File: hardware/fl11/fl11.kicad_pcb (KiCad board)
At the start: 2 copper layers, 187 x 48 mm, 67 parts, among them J1 USB-C 16P, J2_1 TOUCH_SENSE, J2_2 GND, J3_1 TOUCH_SENSE, J3_2 GND, Q1 AO3401A, SW1 BOOT, U1 ESP32-C3-MINI-1-N4, U2 SN74AHCT1G125, U3 AP2112K-3.3, U4 USBLC6-2SC6

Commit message: FL-11 rev E: comb touch electrodes, a fallback header, and the silkscreen that was missing
Correction first: the rev C and rev D commit messages said the silkscreen carried
the name, version and repo URL. It did not. The silk() calls were lost in an
earlier edit and no identity text was on the board at all. They are there now,
verified in the render: name, version, copyright and repo URL, with the
copyright repeated on the snap-off pad so it survives the break.

Interdigitated electrodes, for sensing through plastic. Two solid plates couple
mostly through the overlay's thickness; a comb pushes the field out of the
surface as fringing, which is what a finger behind a cover actually intercepts.
Seven 1.1 mm fingers per electrode on a 3.0 mm pitch, so a ~10 mm fingertip
always spans several SENSE/GND pairs and the delta stays large through a thin
cover instead of collapsing.

J4 gives the escape hatch: four pads, 5V / 3V3 / GND / SIG, next to the break.
A TTP223-class module needs a supply, a ground and one digital output, and
TOUCH_GPIO doubles as that input because touch.py's pin is plain digital rather
than ADC. Both rails are brought out since those modules come in 3.3 V and 5 V
variants. Zero placements, zero BOM lines.

DRC 0 errors, 71 footprints, single-sided, 55 connections still unrouted.

Co-Authored-By: Claude Opus 5 (1M context) <noreply@anthropic.com>
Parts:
- added J4_1: 5V, TestPoint_Pad_D1.0mm, F.Cu at (118.5, 31.0)
- added J4_2: 3V3, TestPoint_Pad_D1.0mm, F.Cu at (118.5, 33.5)
- added J4_3: GND, TestPoint_Pad_D1.0mm, F.Cu at (118.5, 36.0)
- added J4_4: SIG, TestPoint_Pad_D1.0mm, F.Cu at (118.5, 38.5)
- moved TP2 18.6 mm to (109.5, 47.0)
- moved TP3 15.0 mm to (112.5, 47.0)
- moved J2_2 5.00 mm to (117.5, 46.0)
- moved J3_2 5.00 mm to (128.0, 46.0)
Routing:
- net TOUCH_SENSE: track 26.0 -> 23.0 mm
- net GND: track 12.5 -> 9.50 mm
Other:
- outline, holes or cut-outs redrawn
- board text added: "5V 3V3 GND SIG"
- board text added: "CUT TRACES, THEN BEND"
- board text added: "FL-11 rev E TOUCH"
- board text added: "FL-11 rev E · © 2026 Fionn Ferreira"
- board text added: "LINKED FRIEND LIGHTS"
- board text added: "github.com/fionnf/linked-friend-lights-public"
- board text added: "© 2026 Fionn Ferreira"

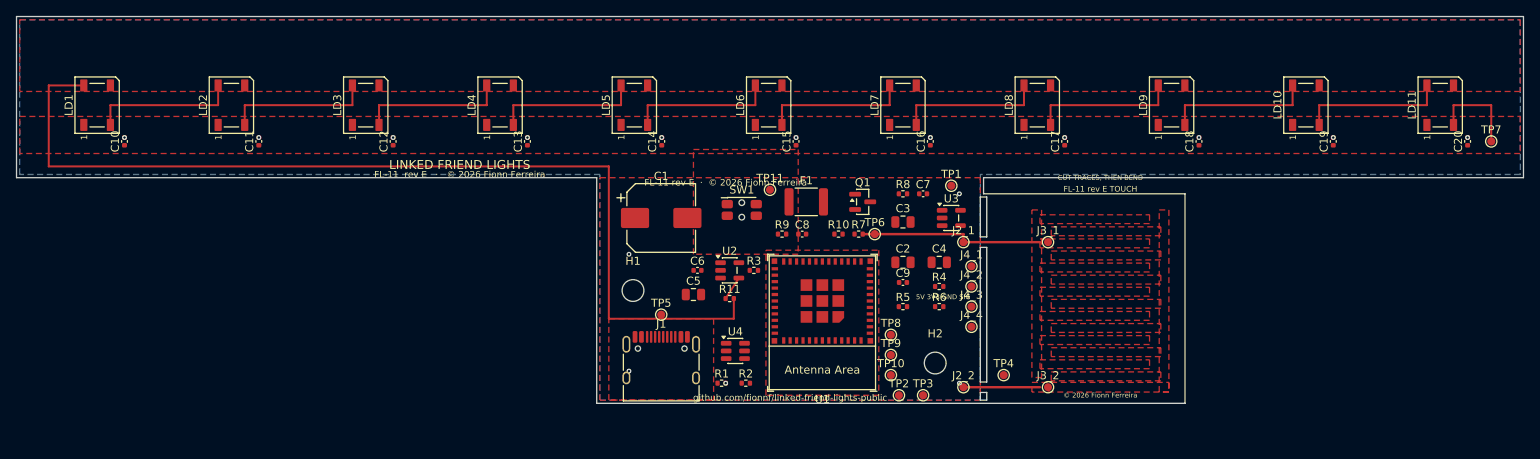
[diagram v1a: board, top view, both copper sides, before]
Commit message: FL-11 rev F: 20 LEDs, and two silent routing bugs fixed
20 LEDs at 8.33333 mm, which is 120 LEDs/m and a standard strip density.
Twenty at that pitch give a lit zone of exactly 166.67 mm -- the same lamp
length as eleven at 60/m, at double the density, so the dots blend. The
outline is unchanged; LED20 lands at x=168.33 on a 187 mm strip.

F1 becomes 3A hold / 5A trip. Twenty LEDs put worst case at ~2.25 A and the
2 A part would nuisance-trip. Same 1812 footprint. Two consequences that are
NOT handled and must not be skipped: the supply has to be 3 A rather than the
2.4 A the cost model assumed, and the copper was sized for 1.6 A -- the 4.6 mm
pour probably carries 2.5 A but that sum has not been redone.

Two routing bugs, both silent, both found only by checking the unconnected
count rather than trusting DRC:

- The DOUT-to-DIN loop was still bounded at 11 after the LED count changed, so
  LEDs 11 through 20 had no data connection at all. Ten hops routed, nine
  missing, zero DRC errors.
- The bypass caps' 5 V pads sat 0.4 mm from the pour edge, too close for
  thermal spokes to form, leaving 23 of them floating. Moved fully inside the
  pour and rotated flat, since at 8.33 mm pitch a vertical 0402 does not fit
  in a 4.6 mm pour with spoke clearance.

Now: all 19 hops routed, all 20 LEDs and all 20 caps connected, 0 DRC errors.
54 endpoints remain unrouted and all of them are in the bulge.

Silkscreen text pulled clear of every board edge and off the notch void.

Co-Authored-By: Claude Opus 5 (1M context) <noreply@anthropic.com>
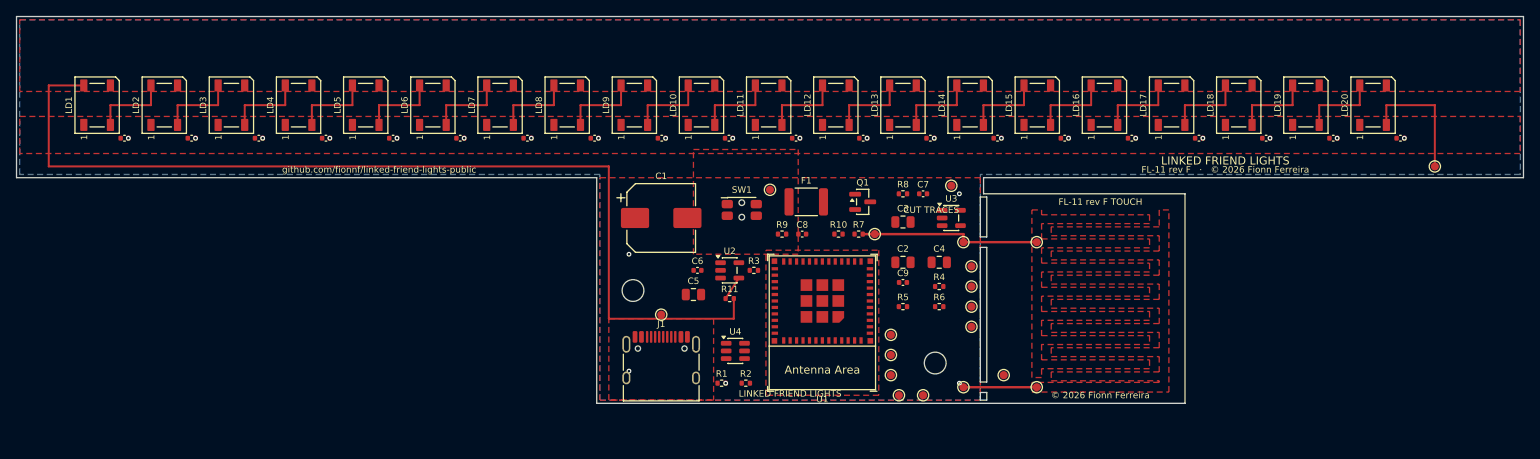
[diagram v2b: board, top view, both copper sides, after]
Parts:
- added C21: 100nF, C_0402_1005Metric, F.Cu at (105.1, 15.1)
- added C22: 100nF, C_0402_1005Metric, F.Cu at (113.4, 15.1)
- added C23: 100nF, C_0402_1005Metric, F.Cu at (121.7, 15.1)
- added C24: 100nF, C_0402_1005Metric, F.Cu at (130.1, 15.1)
- added C25: 100nF, C_0402_1005Metric, F.Cu at (138.4, 15.1)
- added C26: 100nF, C_0402_1005Metric, F.Cu at (146.7, 15.1)
- added C27: 100nF, C_0402_1005Metric, F.Cu at (155.1, 15.1)
- added C28: 100nF, C_0402_1005Metric, F.Cu at (163.4, 15.1)
- added C29: 100nF, C_0402_1005Metric, F.Cu at (171.7, 15.1)
- added LD12: SK6812RGBW, LED_WS2812B_PLCC4_5.0x5.0mm_P3.2mm, F.Cu at (101.7, 11.0)
- added LD13: SK6812RGBW, LED_WS2812B_PLCC4_5.0x5.0mm_P3.2mm, F.Cu at (110.0, 11.0)
- added LD14: SK6812RGBW, LED_WS2812B_PLCC4_5.0x5.0mm_P3.2mm, F.Cu at (118.3, 11.0)
- added LD15: SK6812RGBW, LED_WS2812B_PLCC4_5.0x5.0mm_P3.2mm, F.Cu at (126.7, 11.0)
- added LD16: SK6812RGBW, LED_WS2812B_PLCC4_5.0x5.0mm_P3.2mm, F.Cu at (135.0, 11.0)
- added LD17: SK6812RGBW, LED_WS2812B_PLCC4_5.0x5.0mm_P3.2mm, F.Cu at (143.3, 11.0)
- added LD18: SK6812RGBW, LED_WS2812B_PLCC4_5.0x5.0mm_P3.2mm, F.Cu at (151.7, 11.0)
- added LD19: SK6812RGBW, LED_WS2812B_PLCC4_5.0x5.0mm_P3.2mm, F.Cu at (160.0, 11.0)
- added LD20: SK6812RGBW, LED_WS2812B_PLCC4_5.0x5.0mm_P3.2mm, F.Cu at (168.3, 11.0)
- F1: value PPTC 2A/4A -> PPTC 3A/5A
- moved C20 83.3 mm to (96.7, 15.1), turned to 0 degrees
- moved LD11 83.3 mm to (93.3, 11.0)
- moved C19 75.0 mm to (88.4, 15.1), turned to 0 degrees
- moved LD10 75.0 mm to (85.0, 11.0)
- moved C18 66.7 mm to (80.1, 15.1), turned to 0 degrees
- moved LD9 66.7 mm to (76.7, 11.0)
- moved C17 58.3 mm to (71.7, 15.1), turned to 0 degrees
- moved LD8 58.3 mm to (68.3, 11.0)
- moved C16 50.0 mm to (63.4, 15.1), turned to 0 degrees
- moved LD7 50.0 mm to (60.0, 11.0)
- moved C15 41.7 mm to (55.1, 15.1), turned to 0 degrees
- moved LD6 41.7 mm to (51.7, 11.0)
- moved C14 33.3 mm to (46.7, 15.1), turned to 0 degrees
- moved LD5 33.3 mm to (43.3, 11.0)
- moved C13 25.0 mm to (38.4, 15.1), turned to 0 degrees
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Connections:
- LD11 pad 2: LD11_DOUT -> D_11_12
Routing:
- net D_19_20: track 0.00 -> 9.93 mm
- net D_18_19: track 0.00 -> 9.93 mm
- net D_16_17: track 0.00 -> 9.93 mm
- net D_15_16: track 0.00 -> 9.93 mm
- net D_14_15: track 0.00 -> 9.93 mm
- net D_13_14: track 0.00 -> 9.93 mm
- net D_11_12: track 0.00 -> 9.93 mm
- net D_12_13: track 0.00 -> 9.93 mm
- net D_17_18: track 0.00 -> 9.93 mm
- net D_9_10: track 18.3 -> 9.93 mm
- net D_8_9: track 18.3 -> 9.93 mm
- net D_6_7: track 18.3 -> 9.93 mm
- net D_5_6: track 18.3 -> 9.93 mm
- net D_3_4: track 18.3 -> 9.93 mm
- net D_2_3: track 18.3 -> 9.93 mm
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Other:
- board text added: "CUT TRACES"
- board text added: "FL-11 rev F TOUCH"
- board text added: "FL-11 rev F · © 2026 Fionn Ferreira"
- board text removed: "5V 3V3 GND SIG"
- board text removed: "CUT TRACES, THEN BEND"
- board text removed: "FL-11 rev E TOUCH"
- board text removed: "FL-11 rev E · © 2026 Fionn Ferreira"

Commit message: FL-11 rev G: 15 warm-white LEDs, and the board is routed
15 LEDs at 11.13333 mm. The lit zone stays at exactly 167.00 mm so the lamp
length does not move, and worst case drops to ~1.69 A -- back under the 2 A
PPTC and inside a 2.4 A supply. F1 returns to the 2A/4A part, and both
warnings rev F carried are withdrawn: at 1.69 A the section 5.5 copper sizing
holds with margin.

The LED part was already warm white and now says so. C5378724 is
SKC6812RGBW-WS; the -NW neutral part is C5348912 and would fight
BASE_WARM_WHITE, which is the basis of colour.py's whole model.

Routing is complete: zero unconnected component pads, 345 tracks and 202 vias,
865 mm of copper, 279 segments on F.Cu and 66 on B.Cu.

The bulge was finished with freerouting 2.3.0 through KiCad's Specctra
DSN/SES path. Section 7.9 says not to autoroute and that stands for the three
nets it names, so SENSE, the LED chain, the tab bridges and the pours were
hand-routed first and the router had to work around them. It did: SENSE still
has zero vias and still never crosses the LED data channel.

finish_routing.py fixes what the router got wrong -- 0.15 mm tracks widened to
the 0.20 mm floor, 146 collision-checked stitching vias, ties for the
priority-3 patches the pour clips around, and floating island removal.

Two DRC errors remain and both want a human in the PCB editor, not a script:
a clearance in the 0.5 mm-pitch USB-C fan-out where D+ and D- interleave,
which is precisely the case section 6.2 means by routing D± by hand, and a
STRAP2 via sitting too close to a +3V3 track. Neither is a connectivity
failure.

Co-Authored-By: Claude Opus 5 (1M context) <noreply@anthropic.com>
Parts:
- removed C25, C26, C27, C28, C29: 100nF, C_0402_1005Metric
- removed LD16, LD17, LD18, LD19, LD20: SK6812RGBW, LED_WS2812B_PLCC4_5.0x5.0mm_P3.2mm
- F1: value PPTC 3A/5A -> PPTC 2A/4A
- moved C24 39.2 mm to (169.3, 15.1)
- moved LD15 39.2 mm to (165.9, 11.0)
- moved LD14 36.4 mm to (154.7, 11.0)
- moved C23 36.4 mm to (158.1, 15.1)
- moved C22 33.6 mm to (147.0, 15.1)
- moved LD13 33.6 mm to (143.6, 11.0)
- moved C21 30.8 mm to (135.9, 15.1)
- moved LD12 30.8 mm to (132.5, 11.0)
- moved C20 28.0 mm to (124.7, 15.1)
- moved LD11 28.0 mm to (121.3, 11.0)
- moved TP10 27.4 mm to (100.0, 18.5)
- moved C19 25.2 mm to (113.6, 15.1)
- moved LD10 25.2 mm to (110.2, 11.0)
- moved C18 22.4 mm to (102.5, 15.1)
- moved LD9 22.4 mm to (99.1, 11.0)
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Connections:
- LD15 pad 2: D_15_16 -> LD11_DOUT
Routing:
- net +3V3: track 0.00 -> 88.4 mm, vias 0 -> 4
- net +5V: track 0.00 -> 40.8 mm, vias 0 -> 4
- net VBUS_RAW: track 0.00 -> 39.8 mm, vias 0 -> 4
- net BOOT_N: track 0.00 -> 36.8 mm, vias 0 -> 2
- net VBUS_F: track 0.00 -> 33.9 mm, vias 0 -> 2
- net TOUCH_GPIO: track 0.00 -> 30.8 mm
- net EN: track 0.00 -> 29.3 mm, vias 0 -> 3
- net STRAP8: track 0.00 -> 27.7 mm, vias 0 -> 2
- net UART_TX: track 0.00 -> 22.9 mm, vias 0 -> 2
- net LED_5V: track 0.00 -> 21.7 mm, vias 0 -> 1
- net UART_RX: track 0.00 -> 18.0 mm, vias 0 -> 2
- net USB_DM_CONN: track 0.00 -> 15.6 mm, vias 0 -> 2
- net LED_DATA_3V3: track 0.00 -> 13.9 mm, vias 0 -> 2
- net USB_DP_CONN: track 0.00 -> 12.5 mm, vias 0 -> 2
- net STRAP2: track 0.00 -> 12.4 mm, vias 0 -> 2
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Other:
- board text added: "FL-11 rev G TOUCH"
- board text added: "FL-11 rev G · © 2026 Fionn Ferreira"
- board text removed: "FL-11 rev F TOUCH"
- board text removed: "FL-11 rev F · © 2026 Fionn Ferreira"

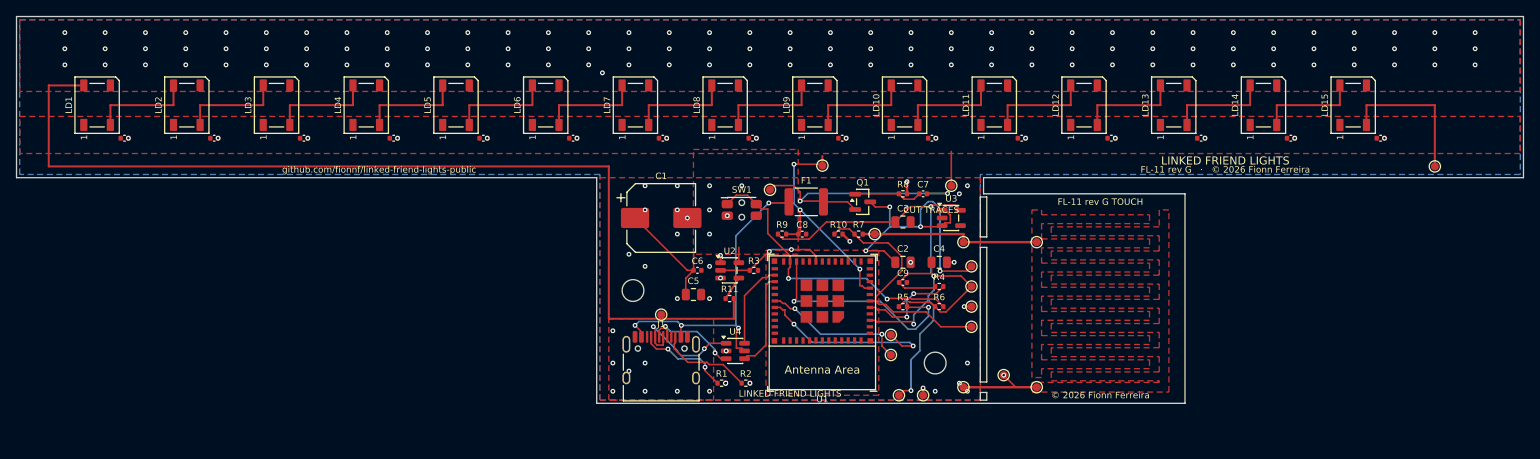
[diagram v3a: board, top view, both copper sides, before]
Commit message: FL-11 rev H: JST plugs, comb fix, fully routed
Three things you asked for, plus a real bug the review caught.

JST-PH plugs on the bulge: J2 for the touch pad pair and J4 for a
commercial sensor, rotated so cables leave along the strip axis in line
with the LEDs. Solder terminals sit beside both, so the board still works
with no connectors at all. The comb block keeps bare copper plus back-side
terminals rather than a plug.

The comb was wrong. SENSE fingers started at 31.6 and GND at 34.6 on a
3.0 mm pitch, which puts them on identical y positions -- stacked, not
interleaved, so half the sensor was shorted geometry rather than a comb.
GND now sits at the half pitch.

J4 carries 5V/GND/SIG with SIG landing on TOUCH_SENSE rather than the GPIO.
A 5V-powered TTP223 drives its output to 5 V and the ESP32-C3 is not 5V
tolerant, so the signal goes in through R7 5.1k and the clamp diode sees
~0.33 mA instead of a direct drive.

GND cannot reach its fingers on the top layer -- the SENSE spine blocks the
full height of the comb -- so it drops to B.Cu down the pad section bare
margin and comes back up into the return bar.

0 DRC errors, 0 unconnected pads.

Co-Authored-By: Claude Opus 5 (1M context) <noreply@anthropic.com>
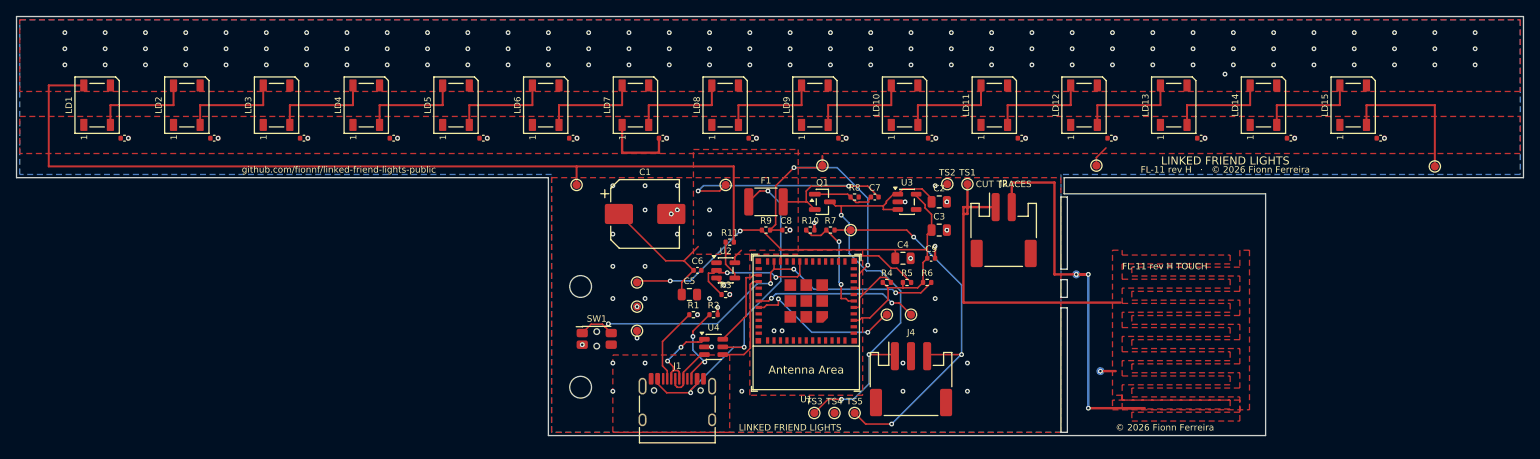
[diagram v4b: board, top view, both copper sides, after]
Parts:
- removed J2_1: TOUCH_SENSE, TestPoint_Pad_D1.0mm
- removed J2_2, J4_3: GND, TestPoint_Pad_D1.0mm
- removed J4_1: 5V, TestPoint_Pad_D1.0mm
- removed J4_2: 3V3, TestPoint_Pad_D1.0mm
- removed J4_4: SIG, TestPoint_Pad_D1.0mm
- added J2: SENSE+GND, JST_PH_S2B-PH-SM4-TB_1x02-1MP_P2.00mm_Horizontal, F.Cu at (122.5, 26.5)
- added J4: 5V/GND/SIG, JST_PH_S3B-PH-SM4-TB_1x03-1MP_P2.00mm_Horizontal, F.Cu at (111.0, 45.0)
- added TS1: TOUCH_SENSE, TestPoint_Pad_D1.0mm, F.Cu at (118.0, 20.8)
- added TS2: GND, TestPoint_Pad_D1.0mm, F.Cu at (115.5, 20.8)
- added TS3: +5V, TestPoint_Pad_D1.0mm, F.Cu at (99.0, 49.2)
- added TS4: GND, TestPoint_Pad_D1.0mm, F.Cu at (101.5, 49.2)
- added TS5: TOUCH_SENSE, TestPoint_Pad_D1.0mm, F.Cu at (104.0, 49.2)
- J3_1, J3_2: moved to B.Cu
- moved TP4 45.8 mm to (77.0, 39.0)
- moved H2 45.0 mm to (70.0, 33.5)
- moved TP3 37.2 mm to (77.0, 36.0)
- moved TP2 35.4 mm to (77.0, 33.0)
- moved SW1 24.1 mm to (72.0, 40.0)
- moved TP5 19.2 mm to (69.5, 20.9)
- moved TP1 18.2 mm to (134.0, 18.5)
- moved J3_1 17.8 mm to (134.5, 44.0)
- moved J3_2 14.8 mm to (131.5, 32.0)
- moved H1 13.6 mm to (70.0, 46.0)
- moved R2 9.39 mm to (86.5, 37.0)
- moved R1 9.19 mm to (84.0, 37.0)
- moved C2 8.75 mm to (114.5, 23.0)
- moved R11 7.00 mm to (88.5, 28.0)
- moved R4 6.52 mm to (108.0, 33.0)
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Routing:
- net TOUCH_SENSE: track 24.5 -> 90.4 mm, vias 0 -> 4
- net GND: track 20.6 -> 56.3 mm, vias 166 -> 170
- net +3V3: track 88.4 -> 66.0 mm, vias 4 -> 2
- net TOUCH_GPIO: track 30.8 -> 14.1 mm, vias 0 -> 2
- net +5V: track 40.8 -> 56.3 mm, vias 4 -> 3
- net BOOT_N: track 36.8 -> 51.4 mm, vias 2 -> 4
- net LED_5V: track 21.7 -> 32.7 mm, vias 1 -> 0
- net LED_DIN1: track 120.8 -> 111.1 mm
- net STRAP8: track 27.7 -> 18.2 mm, vias 2 -> 0
- net EN: track 29.3 -> 38.3 mm, vias 3 -> 2
- net USB_DM_CONN: track 15.6 -> 9.98 mm
- net USB_DP_CONN: track 12.5 -> 7.13 mm, vias 2 -> 0
- net STRAP2: track 12.4 -> 7.10 mm, vias 2 -> 0
- net VBUS_F: track 33.9 -> 38.2 mm
- net VBUS_RAW: track 39.8 -> 43.9 mm, vias 4 -> 3
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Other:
- board size 187 x 48 mm -> 187 x 52 mm
- board text added: "FL-11 rev H TOUCH"
- board text added: "FL-11 rev H · © 2026 Fionn Ferreira"
- board text removed: "FL-11 rev G TOUCH"
- board text removed: "FL-11 rev G · © 2026 Fionn Ferreira"
